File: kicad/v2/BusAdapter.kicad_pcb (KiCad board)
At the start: 2 copper layers, 99.1 x 99.1 mm, 50 parts, among them J1 Conn_02x17_Odd_Even, J10 Conn_02x06_Odd_Even, J11 Conn_02x02_Odd_Even, J2 Conn_02x20_Odd_Even, J3 Conn_02x20_Odd_Even, J4 Conn_02x06_Top_Bottom, J5 Conn_02x06_Top_Bottom, J6 Conn_Coaxial, J7 Conn_Coaxial, J8 Conn_01x02_Male, J9 Conn_01x02_Male, Q1 2N3904, Q2 2N3904, SW1 SW_Push, SW2 SW_Push, U1 74LVC245, U2 74LVC245, U3 74LVC245, U4 IS61C5128AL-10TLI, U5 MCP4822

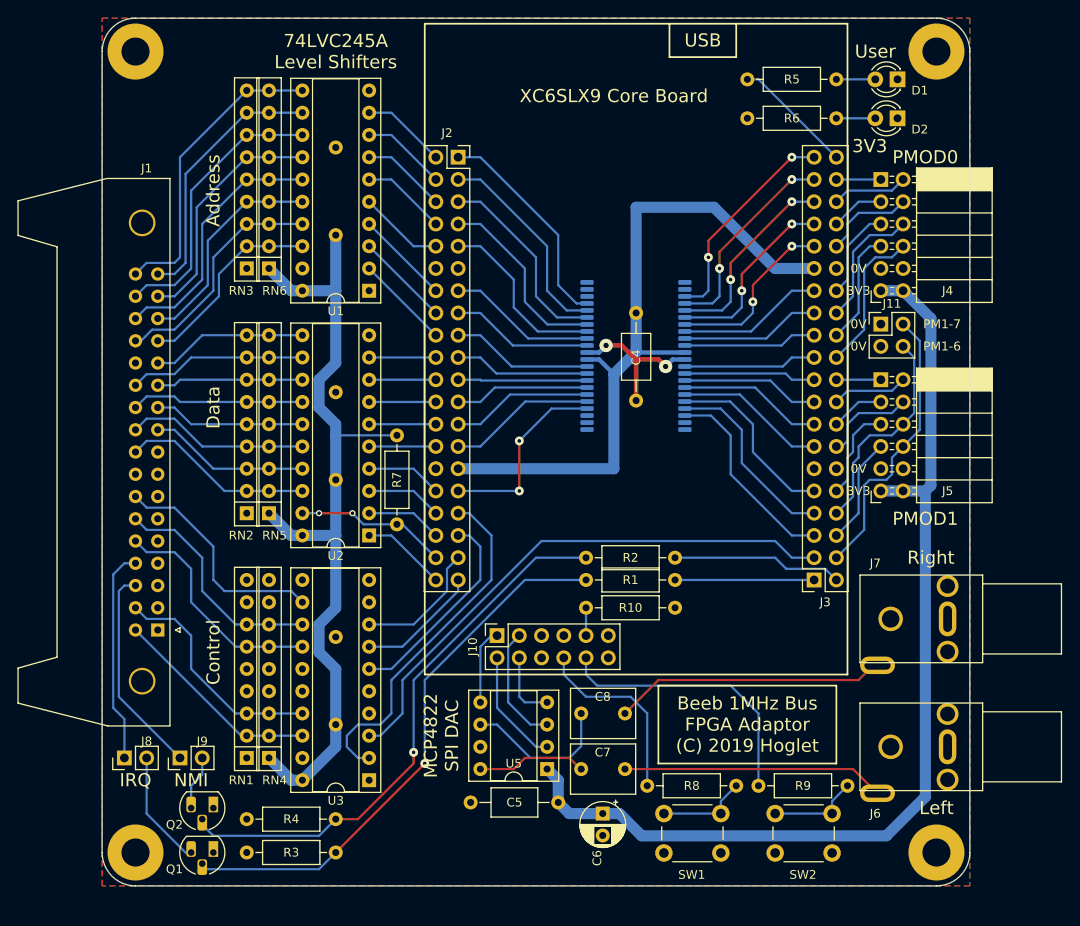
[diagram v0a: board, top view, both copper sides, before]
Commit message: PCB v2: Added pmod2 and updated layout
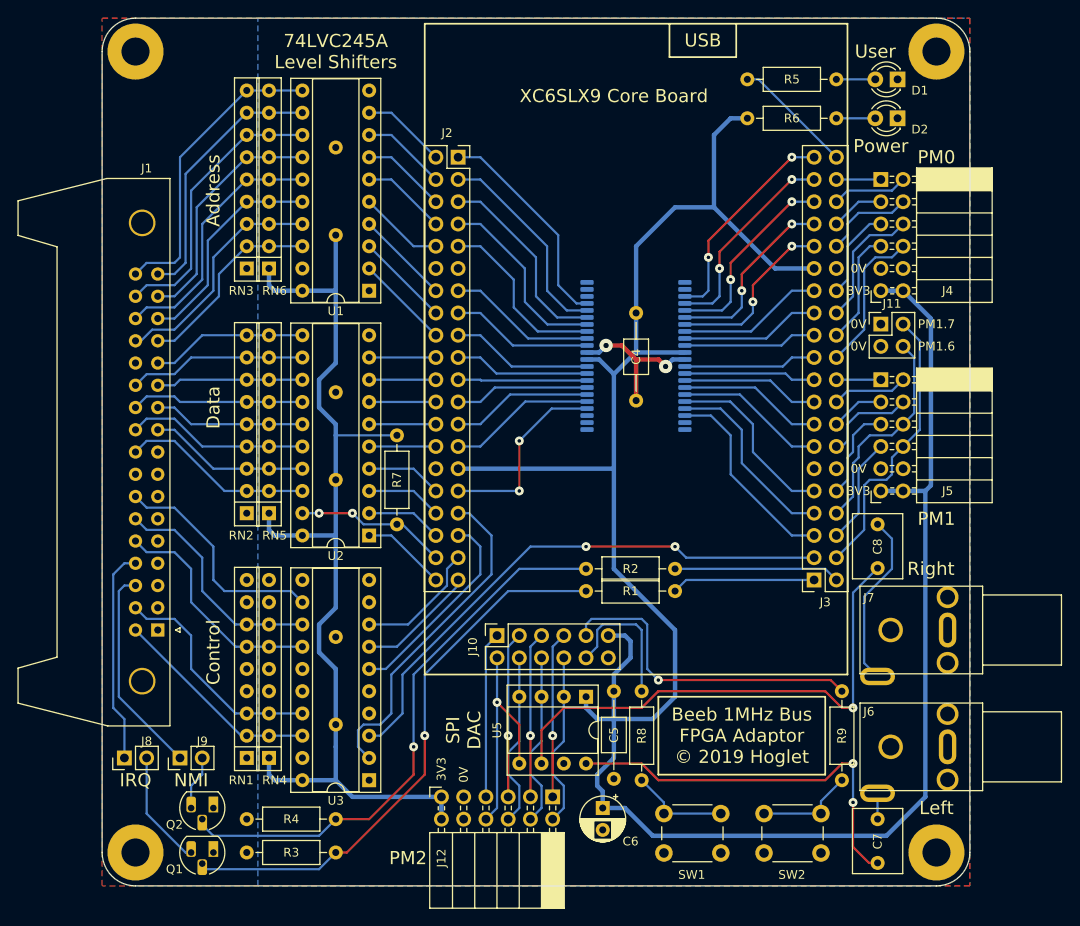
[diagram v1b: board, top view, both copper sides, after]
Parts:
- removed R10: 1K0, Resistor_THT:R_Axial_DIN0207_L6.3mm_D2.5mm_P10.16mm_Horizontal
- added J12: Conn_02x06_Top_Bottom, footprints:PinSocket_2x06_P2.54mm_Horizontal, F.Cu at (89.2, 138.7)
- C1, C2, C3, C4, C5: footprint Capacitor_THT:C_Axial_L5.1mm_D3.1mm_P10.00mm_Horizontal -> Capacitor_THT:C_Axial_L3.8mm_D2.6mm_P10.00mm_Horizontal
- moved C8 36.0 mm to (139.0, 107.6), turned to 270 degrees
- moved C7 29.4 mm to (139.0, 141.3), turned to 270 degrees
- moved R9 14.4 mm to (134.9, 126.7), turned to 270 degrees
- moved C5 14.2 mm to (108.9, 126.7), turned to 270 degrees
- moved R8 10.8 mm to (112.1, 126.7), turned to 270 degrees
- moved U5 9.38 mm to (105.7, 127.3), turned to 270 degrees
- moved SW2 1.27 mm to (126.0, 140.6)
- moved J7 1.27 mm to (147.0, 119.7)
- moved R1 1.27 mm to (105.7, 115.2)
- moved R2 1.27 mm to (105.7, 112.7)
- moved C6 0.63 mm to (107.6, 140.0)
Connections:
- net /DAC_SDI renamed /PMOD2_6
- J10 pad 1: /DAC_LDAC -> /PMOD2_3
- J10 pad 10: /SW2 -> /SW1
- J10 pad 2: /DAC_CS -> /PMOD2_7
- J10 pad 3: /DAC_SCK -> /PMOD2_2
- J10 pad 5: Net-(J10-Pad5) -> /PMOD2_1
- J10 pad 6: Net-(J10-Pad6) -> /PMOD2_5
- J10 pad 7: Net-(J10-Pad7) -> /PMOD2_0
- J10 pad 8: /SW1 -> /PMOD2_4
- J10 pad 9: /HSWAPEN -> /SW2
- U5 pad 2: /DAC_CS -> /PMOD2_4
- U5 pad 3: /DAC_SCK -> /PMOD2_5
- U5 pad 5: /DAC_LDAC -> /PMOD2_7
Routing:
- net +3V3: track 294.1 -> 381.2 mm
- net Net-(C8-Pad2): track 17.5 -> 59.2 mm, vias 0 -> 1
- net Net-(C7-Pad2): track 12.6 -> 45.1 mm, vias 0 -> 2
- net /PMOD2_7: track 0.00 -> 27.0 mm, vias 0 -> 1
- net Net-(C7-Pad1): track 30.0 -> 3.32 mm
- net /PMOD2_5: track 0.00 -> 20.0 mm
- net /PMOD2_4: track 0.00 -> 20.0 mm
- net /PMOD2_1: track 0.00 -> 18.9 mm, vias 0 -> 1
- net /PMOD2_3: track 0.00 -> 18.9 mm
- net /PMOD2_2: track 0.00 -> 18.9 mm, vias 0 -> 1
- net /PMOD2_0: track 0.00 -> 18.9 mm, vias 0 -> 1
- net /DAC_SCK: track 13.6 -> 0.00 mm
- net /DAC_CS: track 13.3 -> 0.00 mm
- net /PMOD2_6: track 7.88 -> 20.0 mm
- net Net-(C8-Pad1): track 31.1 -> 20.0 mm
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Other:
- board text added: "Beeb 1MHz Bus FPGA Adaptor © 2019 Hoglet"
- board text added: "PM0"
- board text added: "PM1"
- board text added: "PM1.6"
- board text added: "PM1.7"
- board text added: "PM2"
- board text added: "Power"
- board text added: "SPI DAC"
- board text removed: "Beeb 1MHz Bus FPGA Adaptor (C) 2019 Hoglet"
- board text removed: "MCP4822 SPI DAC"
- board text removed: "PM1-6"
- board text removed: "PM1-7"
- board text removed: "PMOD0"
- board text removed: "PMOD1"

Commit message: PCB v2: Updated SW1/2 to HSWAPEN pulled low on power up
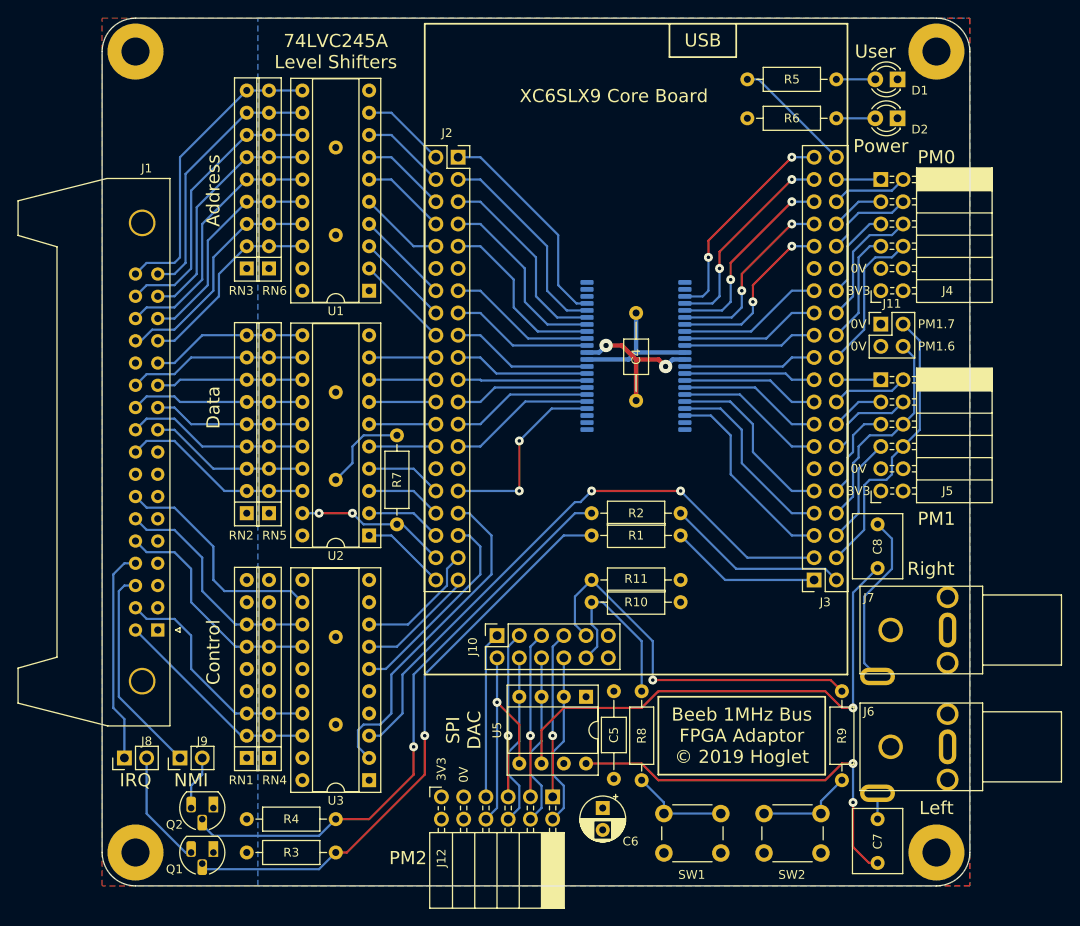
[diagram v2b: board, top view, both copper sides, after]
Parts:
- added R10: 1K, Resistor_THT:R_Axial_DIN0207_L6.3mm_D2.5mm_P10.16mm_Horizontal, F.Cu at (106.3, 116.5)
- added R11: 1K, Resistor_THT:R_Axial_DIN0207_L6.3mm_D2.5mm_P10.16mm_Horizontal, F.Cu at (106.3, 114.0)
- moved R8 10.2 mm to (112.1, 136.8), turned to 90 degrees
- moved R9 10.2 mm to (134.9, 136.8), turned to 90 degrees
- moved R2 6.38 mm to (106.3, 106.3)
- moved R1 6.38 mm to (106.3, 108.9)
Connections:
- R8 pad 1: /SW1 -> Net-(R8-Pad1)
- R8 pad 2: Net-(R8-Pad2) -> /SW1
- R9 pad 1: /SW2 -> Net-(R9-Pad1)
- R9 pad 2: Net-(R9-Pad2) -> /SW2
- SW1 pad 1: Net-(R8-Pad2) -> Net-(R8-Pad1)
- SW1 pad 2: GND -> +3V3
- SW2 pad 1: Net-(R9-Pad2) -> Net-(R9-Pad1)
- SW2 pad 2: GND -> +3V3
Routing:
- net +3V3: track 381.2 -> 26.2 mm
- net Net-(R8-Pad2): track 11.4 -> 0.00 mm
- net Net-(R8-Pad1): track 0.00 -> 11.4 mm
- net Net-(R9-Pad2): track 11.3 -> 0.00 mm
- net Net-(R9-Pad1): track 0.00 -> 11.3 mm
- net /SW2: track 37.1 -> 44.1 mm
- net /LV_1MHZE: track 62.9 -> 68.1 mm
- net /SW1: track 16.3 -> 20.4 mm
- net Net-(Q2-Pad2): track 64.3 -> 67.6 mm
- net Net-(Q1-Pad2): track 63.7 -> 66.9 mm
- net /LV_NMI: track 18.9 -> 20.9 mm
- net /LV_IRQ: track 16.4 -> 17.3 mm

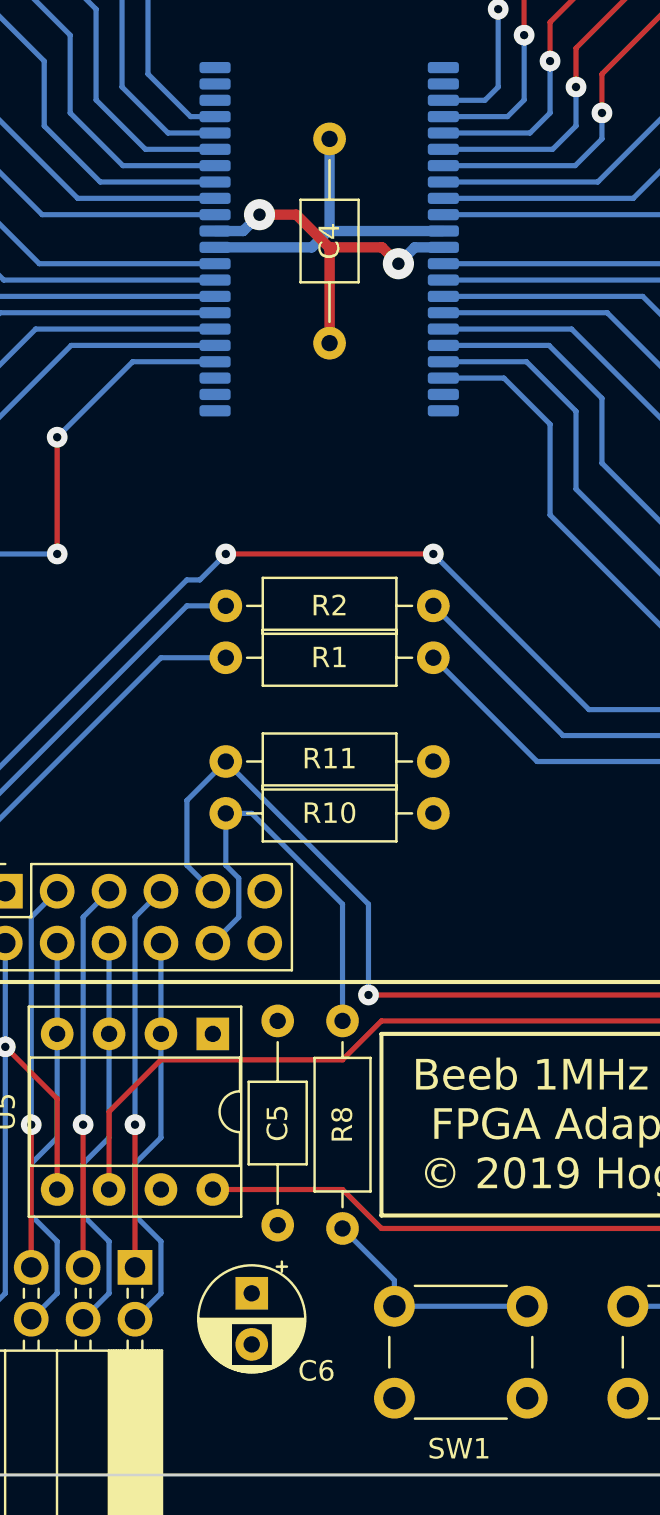
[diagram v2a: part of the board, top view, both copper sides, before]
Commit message: PCB v2: Improved SRAM decoupling
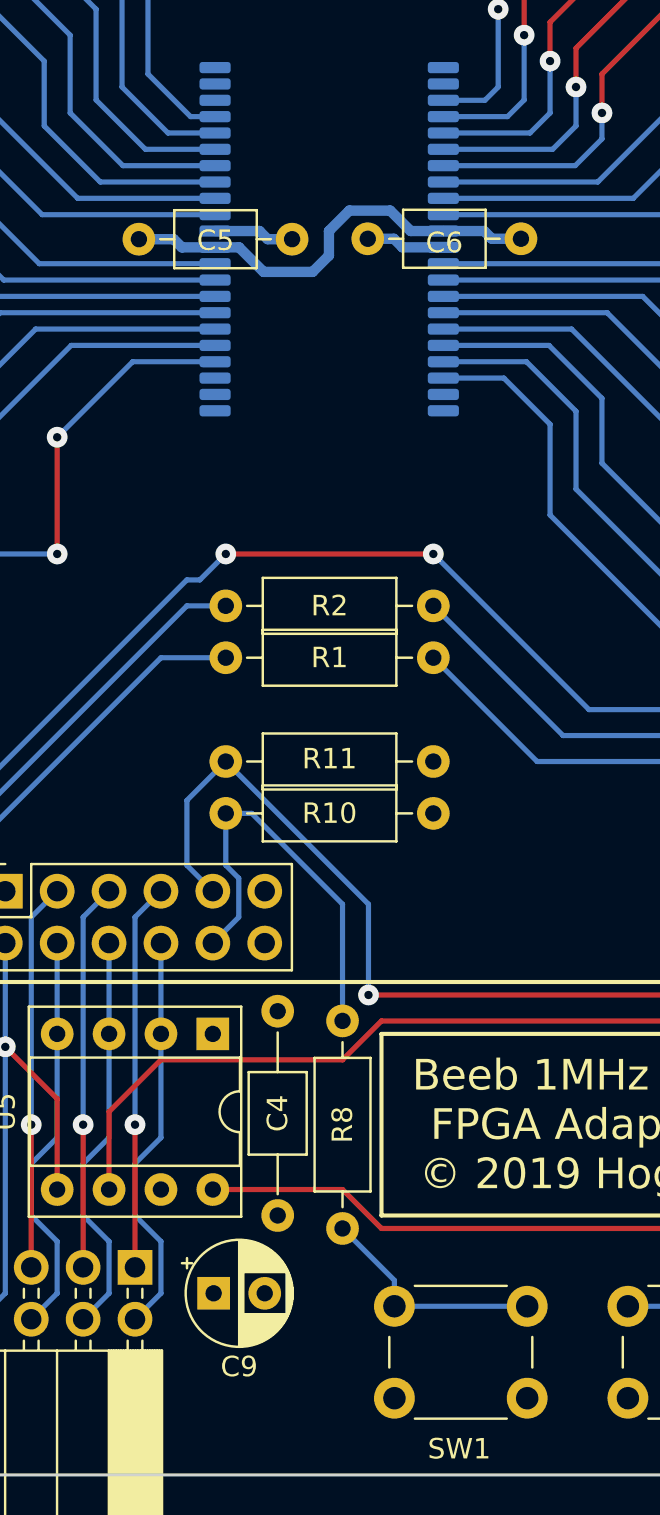
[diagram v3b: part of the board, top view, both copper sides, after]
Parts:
- added C9: 10u, Capacitor_THT:CP_Radial_D5.0mm_P2.50mm, F.Cu at (105.8, 140.0)
- C5: footprint Capacitor_THT:C_Axial_L3.8mm_D2.6mm_P10.00mm_Horizontal -> Capacitor_THT:C_Axial_L3.8mm_D2.6mm_P7.50mm_Horizontal
- C6: value 10u -> 100n; footprint Capacitor_THT:CP_Radial_D5.0mm_P2.50mm -> Capacitor_THT:C_Axial_L3.8mm_D2.6mm_P7.50mm_Horizontal
- moved C6 53.3 mm to (120.8, 88.4), turned to 180 degrees
- moved C4 42.8 mm to (108.9, 126.2)
- moved C5 38.9 mm to (102.1, 88.4), turned to 0 degrees
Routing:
- net GND: track 17.5 -> 7.81 mm, vias 2 -> 0
- net +3V3: track 26.2 -> 32.1 mm

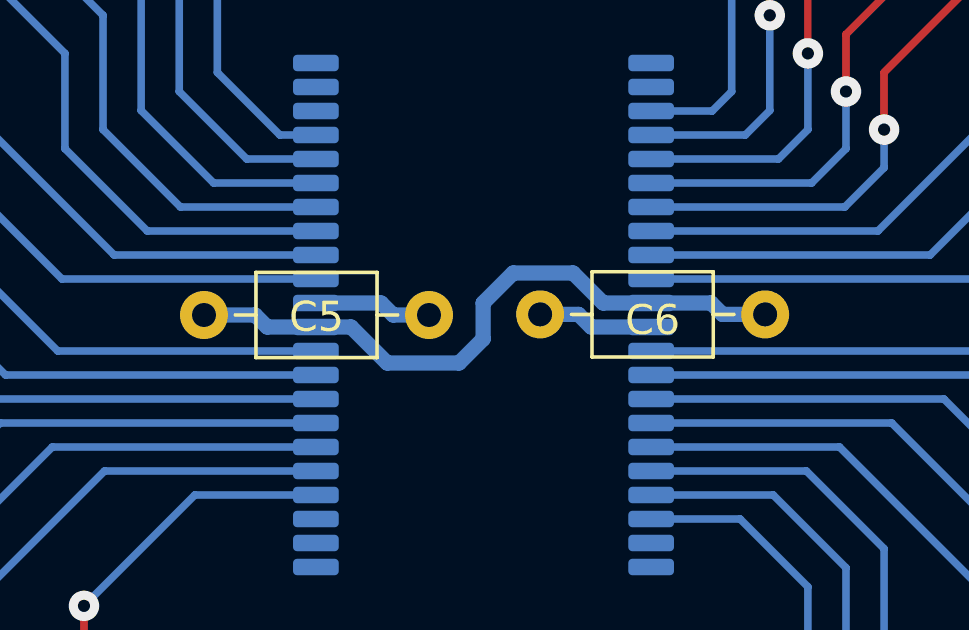
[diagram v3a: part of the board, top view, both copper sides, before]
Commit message: PCB v2: Improved SRAM decoupling even more
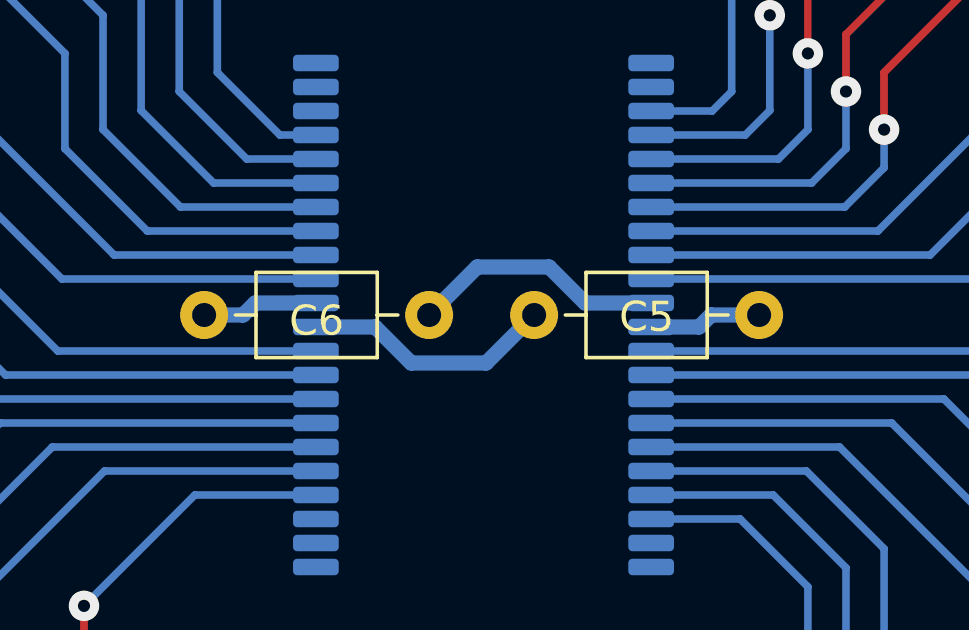
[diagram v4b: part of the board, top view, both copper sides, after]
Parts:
- moved C6 11.2 mm to (109.6, 88.4)
- moved C5 11.0 mm to (113.1, 88.4)
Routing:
- net +3V3: track 32.1 -> 27.2 mm

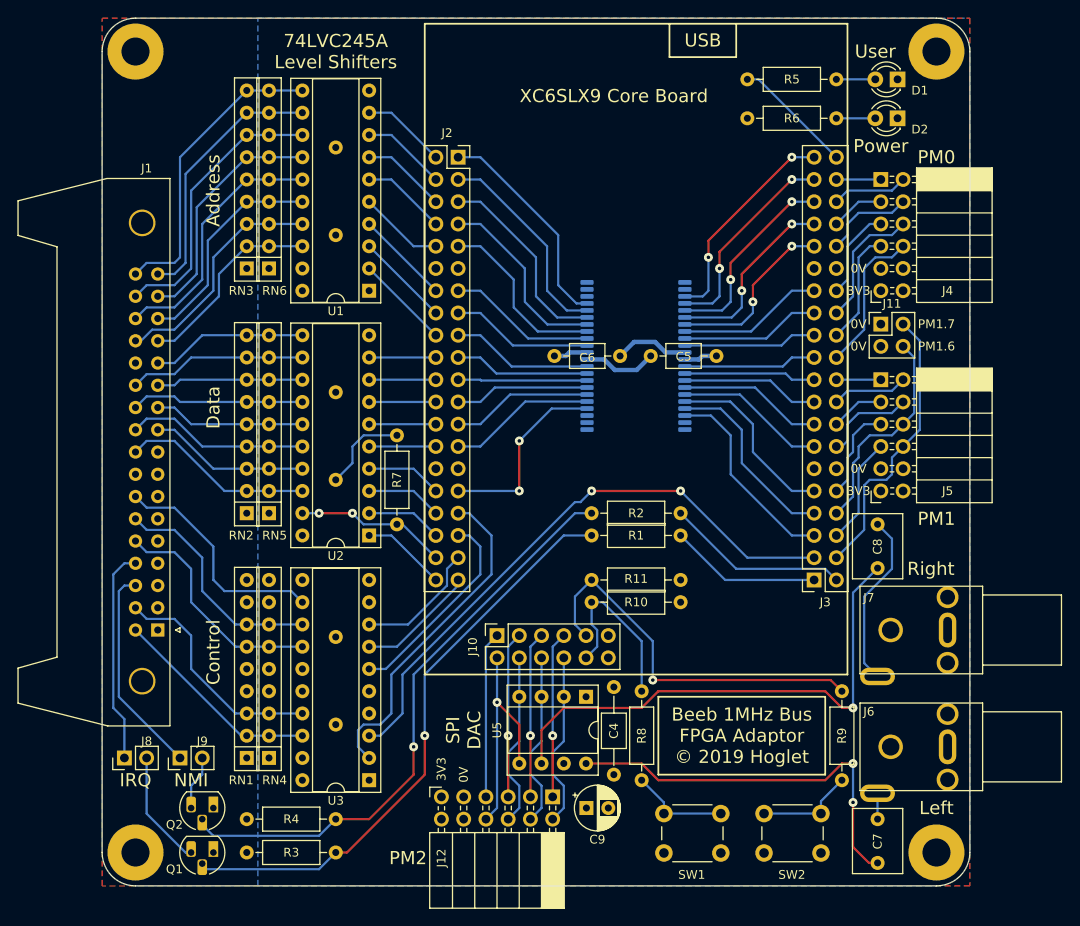
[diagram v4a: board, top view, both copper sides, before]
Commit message: PCB v2: Enlarged IDC connector holes; added power connector
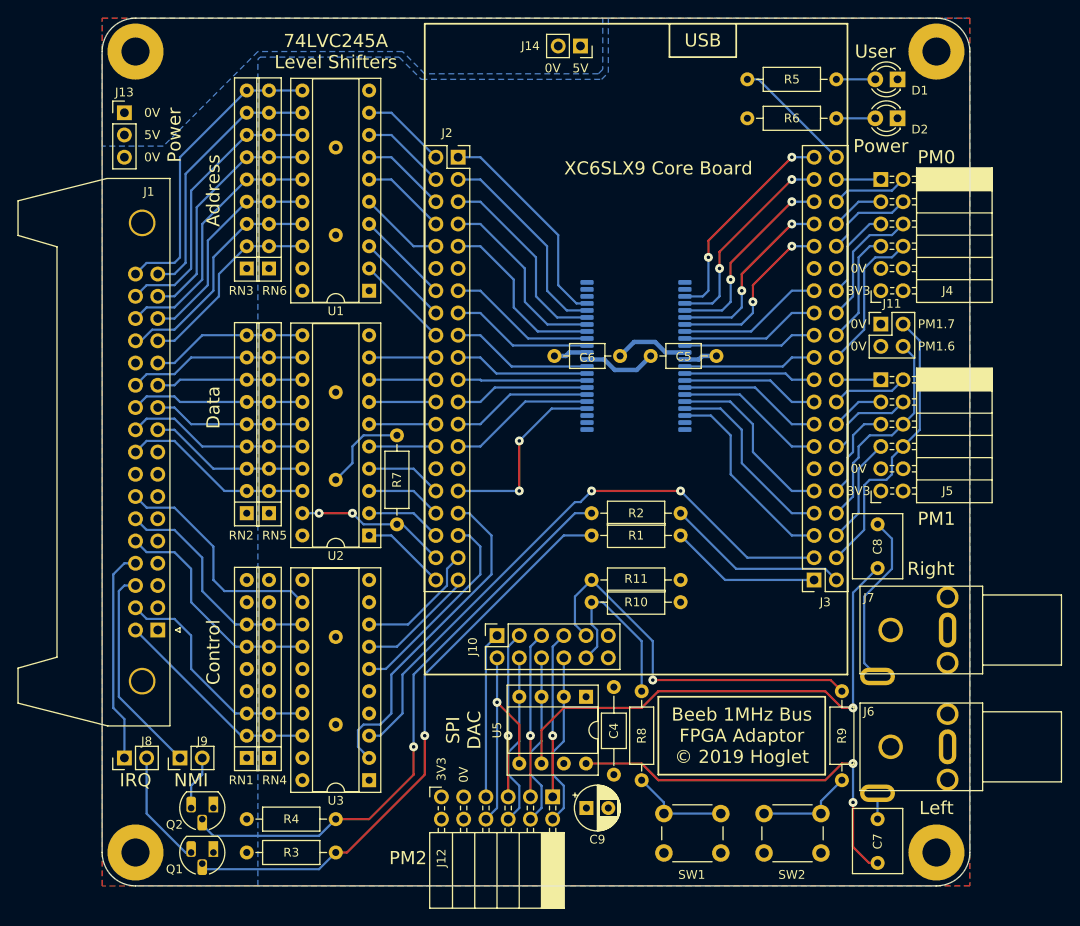
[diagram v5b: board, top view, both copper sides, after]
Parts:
- added J13: Conn_01x03, Connector_PinHeader_2.54mm:PinHeader_1x03_P2.54mm_Vertical, F.Cu at (53.0, 60.6)
- added J14: Conn_01x02, Connector_PinSocket_2.54mm:PinSocket_1x02_P2.54mm_Vertical, F.Cu at (105.1, 53.0)
- J1: footprint Connector_IDC:IDC-Header_2x17_P2.54mm_Horizontal_Lock -> footprints:IDC-Header_2x17_P2.54mm_Horizontal_Lock
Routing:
- added copper zone on B.Cu, net +5V
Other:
- board text added: "5V"
